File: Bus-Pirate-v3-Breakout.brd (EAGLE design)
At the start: 21.3 x 27.7 mm, 9 parts

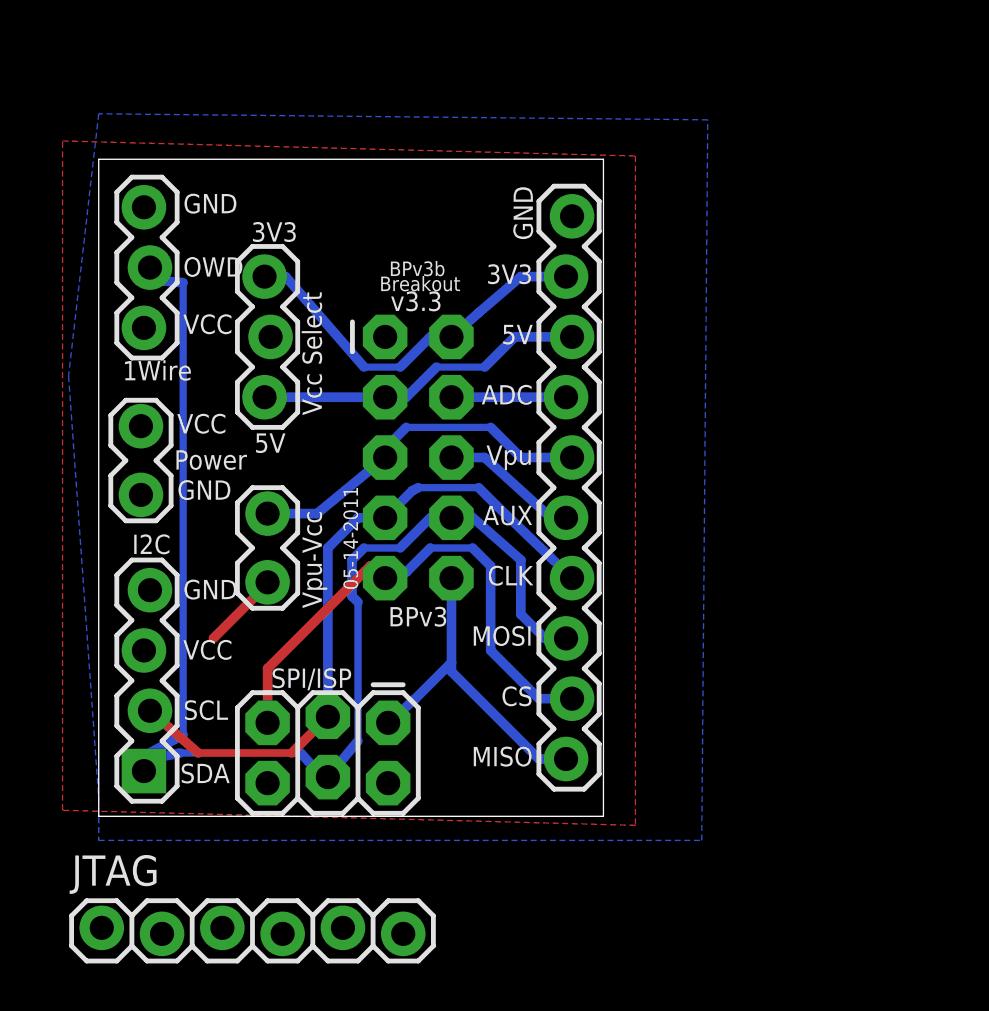
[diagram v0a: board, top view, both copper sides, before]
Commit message: Clean up and add panelization config
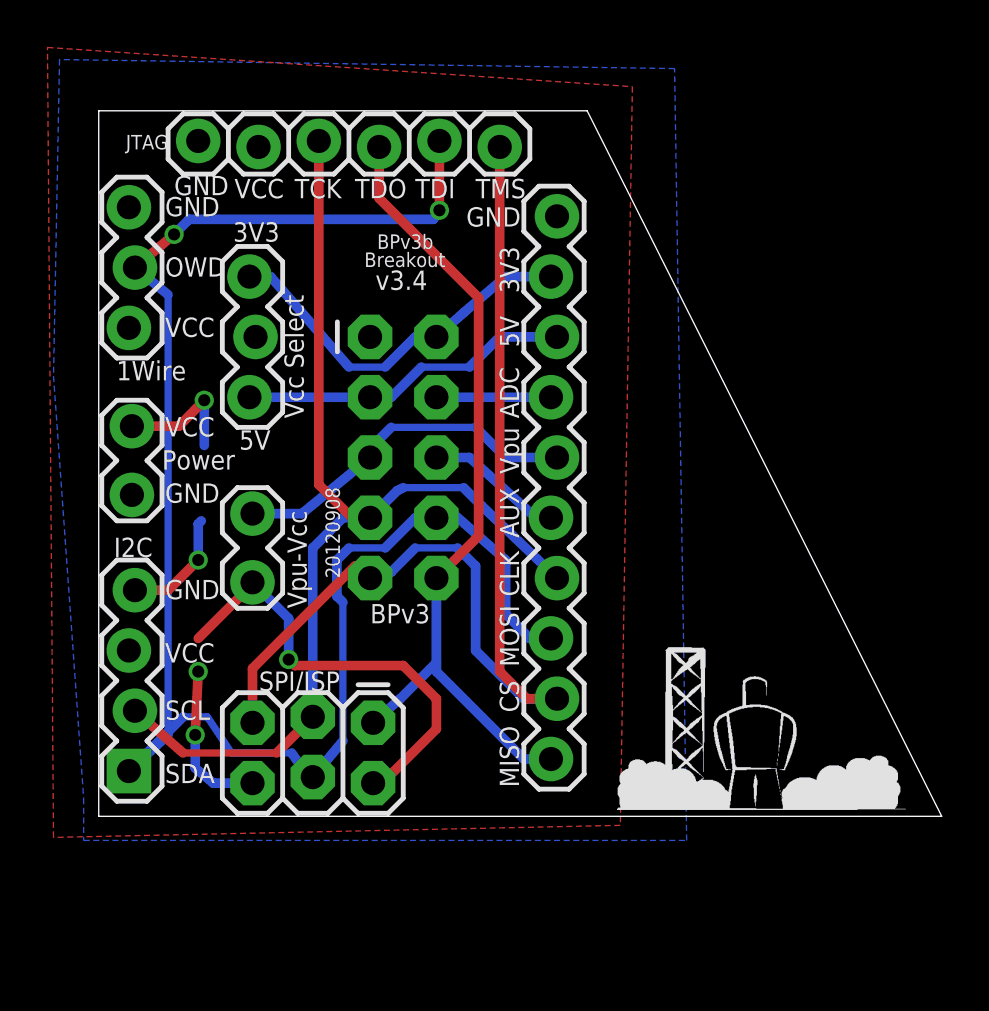
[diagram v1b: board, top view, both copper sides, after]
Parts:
- added U$2: LOGO_SPACE_AGE_ROBOTICS0.48*0.27, logos:LOGO_SPACE_AGE_ROBOTICS_SMALL_0.48X0.27
- moved JTAG 36.9 mm to (16.9, 28.2), turned to 180 degrees
- moved BREADBOARD 0.64 mm to (19.2, 25.3)
- moved 1-WIRE 0.64 mm to (1.40, 20.6)
- moved I2C 0.64 mm to (1.40, 1.91)
- moved BUS_PIRATE 0.63 mm to (12.8, 15.1)
- moved PULLUP 0.63 mm to (6.48, 12.6)
- moved SPI/ISP 0.63 mm to (11.6, 3.94)
- moved VCC_SELECT 0.63 mm to (6.48, 17.7)
- moved POWER 0.38 mm to (1.40, 16.3)
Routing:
- net CS: track 22.2 -> 47.2 mm
- net MISO: track 14.0 -> 34.6 mm
- net MOSI: track 55.4 -> 72.6 mm, vias 0 -> 2
- net CLK: track 28.8 -> 46.0 mm
- net GND: track 0.00 -> 17.0 mm, vias 0 -> 4
- net VCC: track 3.31 -> 19.0 mm, vias 0 -> 1
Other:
- board size 21.3 x 27.7 mm -> 35.5 x 29.7 mm
- board text added: "20120908"
- board text added: "JTAG"
- board text added: "TCK"
- board text added: "TDI"
- board text added: "TDO"
- board text added: "TMS"
- board text added: "v3.4"
- board text removed: "05-14-2011"
- board text removed: "v3.3"
